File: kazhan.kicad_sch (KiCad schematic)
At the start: 94 parts, among them J1 AudioJack4, J2 AudioJack4, J3 USB_C_Receptacle_USB2.0, SW3 BOOT, SW4 RESET, U2 CH552T, U3 CH552T, U4 USBLC6-2SC6, U5 CH552T

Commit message: outline and placing started
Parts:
- removed H6: Mounting_Hole, symbol ScottoKeebs:Placeholder_Mounting_Hole
- added U1: USBLC6-2SC6, Package_TO_SOT_SMD:SOT-23-6, symbol Power_Protection:USBLC6-2SC6
- H1, H2, H3, H4, H5: footprint (none) -> MyFootprintsCollection:MountingHole_3.5mmX4.5mm_Pad
- J1: footprint MyFootprintsCollection:CON_MJ-4PP-9_Reversible -> MyFootprintsCollection:PJ-320A-REVERSIBLE-F.Cu-placing
- J2: footprint MyFootprintsCollection:CON_MJ-4PP-9_Reversible -> MyFootprintsCollection:PJ-320A-REVERSIBLE-B.Cu-placing
- JP10, JP14, JP18, JP6: footprint Jumper:SolderJumper-2_P1.3mm_Open_RoundedPad1.0x1.5mm -> MyFootprintsCollection:SolderJumper-EdgeCut-B.Cu-Placing
- JP13, JP17, JP5, JP9: footprint Jumper:SolderJumper-2_P1.3mm_Open_RoundedPad1.0x1.5mm -> MyFootprintsCollection:SolderJumper-EdgeCut-F.Cu-Placing
- JP23: footprint Jumper:SolderJumper-2_P1.3mm_Open_RoundedPad1.0x1.5mm -> MyFootprintsCollection:SolderJumper-F.Cu-B.Cu
- S1, S10, S11, S12, S13, S14, S15, S16, S17, S18, S19, S2, S20, S21, S22, S23, S24, S25, S26, S27, S28, S3, S4, S5, S6, S7, S8, S9: footprint MyFootprintsCollection:SW_Hotswap_Kailh_Choc_MX_1.00u -> MyFootprintsCollection:SW_Hotswap_Kailh_Choc_MX_1.00u_One_Sided
- U5: footprint Package_SO:TSSOP-20_4.4x6.5mm_P0.65mm -> MyFootprintsCollection:TSSOP-20_4.4x6.5mm_P0.65mm-REVERSIBLE
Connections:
- net GND: now also J1.S, J2.S, U1.2 (GND)
- net VCC: now also J1.T, J2.T, U1.5 (VBUS)
- net at J1.R1: now also U1.6 (I/O1)
- net at J1.R2: now also U1.4 (I/O2)
- net R_RX: now reaches U2.10 (P30)
- net R_RX: now also J2.R2
- net R_TX: now reaches U2.9 (P31)
- net R_TX: now also J2.R1
- net at SW1.1 (IN): now also D11.2 (A); no longer D15.2 (A)
- net at SW1.5 (IN): now also D15.2 (A); no longer D11.2 (A)
- net RX renamed L_RX
- net L_RX: now also U1.1 (I/O1)
- net TX renamed L_TX
- net L_TX: now also U1.3 (I/O2)
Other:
- note added: "SIDE B.Cu"
- note added: "SIDE F.Cu"
- note added: "UART ESD protection"
- note added: "left R1:RX, R2:TX"
- note added: "right R1:TX, R2:RX"
- note removed: "B.Cu"
- note removed: "F.Cu"
- moved on the sheet: C1, C2, D17, D18, D19, F1, JP23, R1, R4, R5, SW1, SW2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

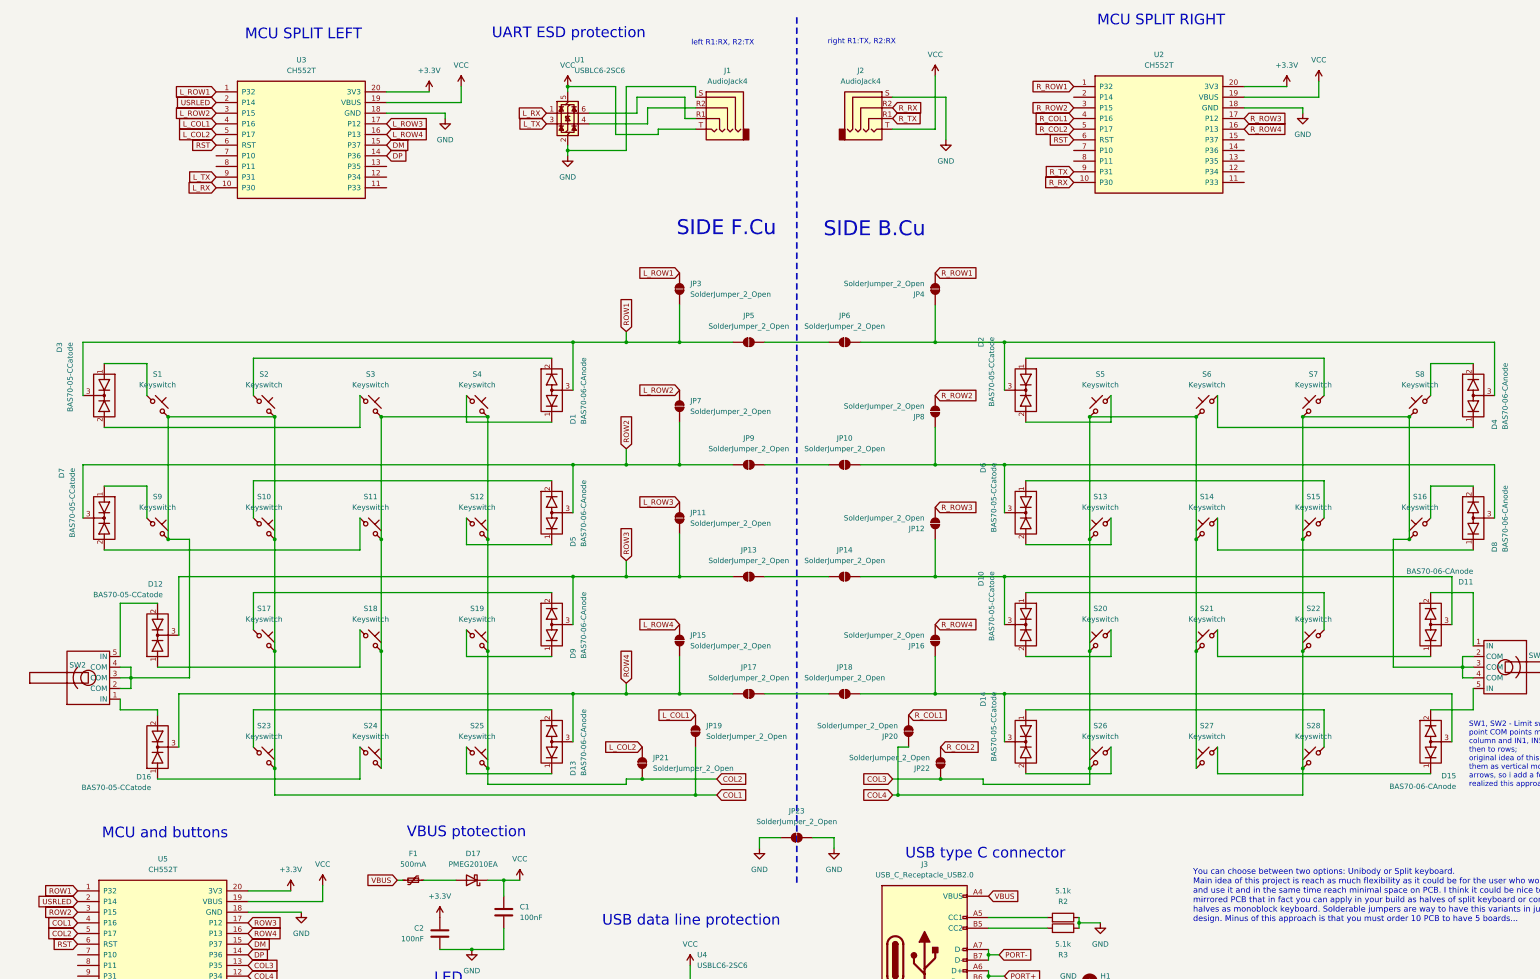
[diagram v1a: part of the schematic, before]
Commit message: all except matrix is routed
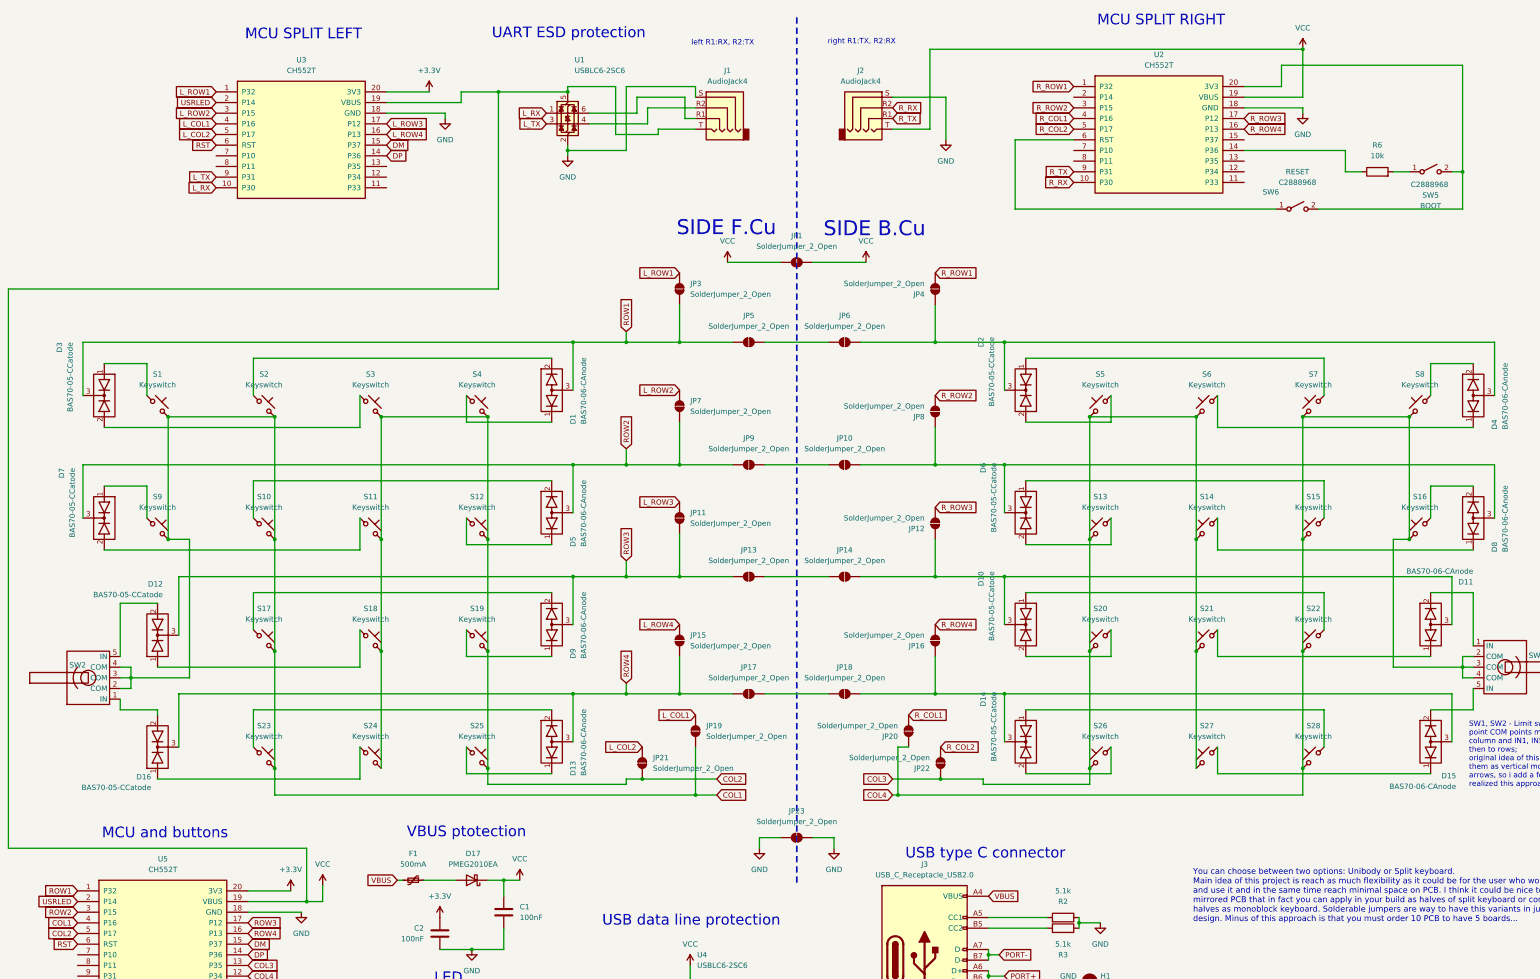
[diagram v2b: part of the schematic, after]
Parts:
- added JP1: SolderJumper_2_Open, MyFootprintsCollection:SolderJumper-F.Cu-B.Cu, symbol Jumper:SolderJumper_2_Open
- added R6: 10k, Resistor_SMD:R_0402_1005Metric_Pad0.72x0.64mm_HandSolder, symbol Device:R
- added SW5: BOOT, MyFootprintsCollection:KEY-SMD_4P-L4.8-W4.8-P3.70-LS6.4-TL, symbol Switch:SW_SPST
- added SW6: RESET, MyFootprintsCollection:KEY-SMD_4P-L4.8-W4.8-P3.70-LS6.4-TL, symbol Switch:SW_SPST
- JP10, JP14, JP18, JP6: footprint MyFootprintsCollection:SolderJumper-EdgeCut-B.Cu-Placing -> MyFootprintsCollection:SolderJumper-1.25x0.5
- JP11, JP12, JP15, JP16, JP19, JP20, JP21, JP22, JP3, JP4, JP7, JP8: footprint Jumper:SolderJumper-2_P1.3mm_Open_RoundedPad1.0x1.5mm -> MyFootprintsCollection:SolderJumper-1.25x0.5
- JP13, JP17, JP5, JP9: footprint MyFootprintsCollection:SolderJumper-EdgeCut-F.Cu-Placing -> MyFootprintsCollection:SolderJumper-1.25x0.5
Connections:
- net +3.3V: no longer U2.20 (3V3)
- net RST: no longer U2.6 (RST)
- net VCC: now also JP1.1 (A), JP1.2 (B)
- net at U2.14 (P36): now also R6.1
- new net: SW5.2 (B), SW6.2 (B), U2.20 (3V3)
- new net: SW6.1 (A), U2.6 (RST)
- new net: R6.2, SW5.1 (A)

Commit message: upd readme
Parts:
- SW1, SW2: LCSC (none) -> C470322
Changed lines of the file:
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@@
+			)
+		)
+		(property "LCSC" "C470322"
+			(at 369.57 179.07 90)
+			(effects
+				(font
+					(size 1.27 1.27)
+				)
+				(hide yes)
 			)
 		)
@@
 			(effects
 				(font
+					(size 1.27 1.27)
+				)
+				(hide yes)
+			)
+		)
+		(property "LCSC" "C470322"
+			(at 41.91 181.61 90)
+			(effects
+				(font
